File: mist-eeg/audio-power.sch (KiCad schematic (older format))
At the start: 18 parts, among them U2 LT3042xMSE, U3 LT3042xMSE

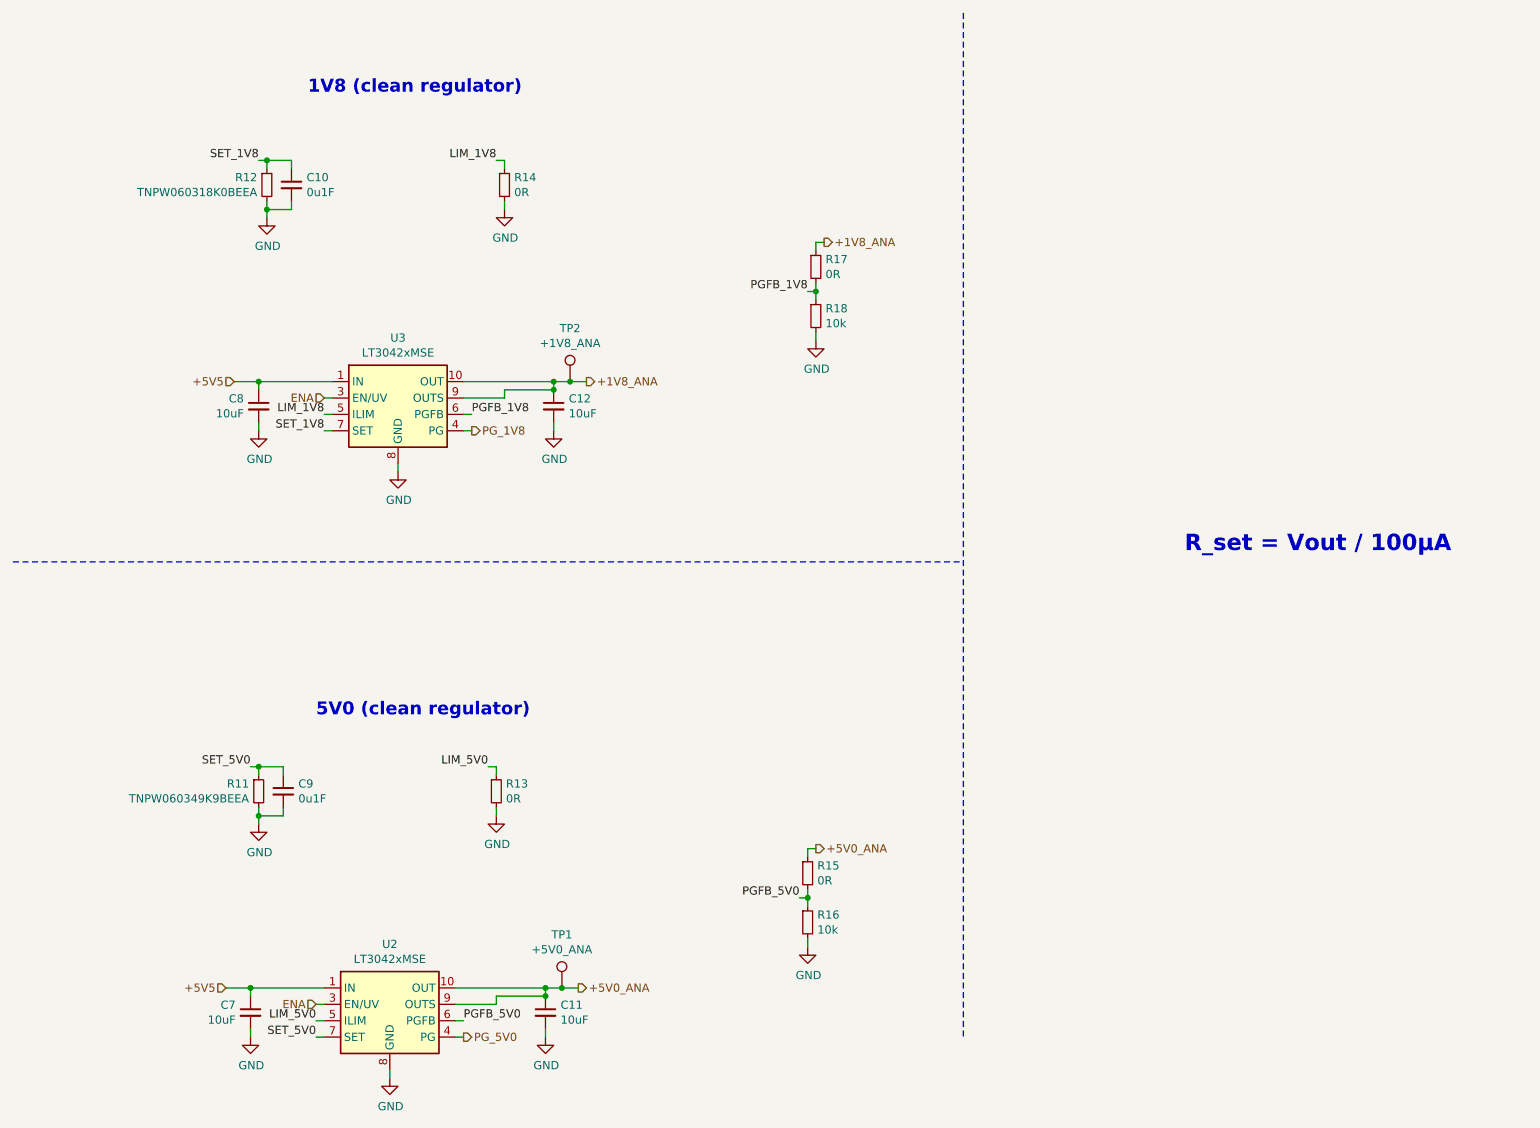
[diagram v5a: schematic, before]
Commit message: Switch to POL switching regulator to accelerate production of the board
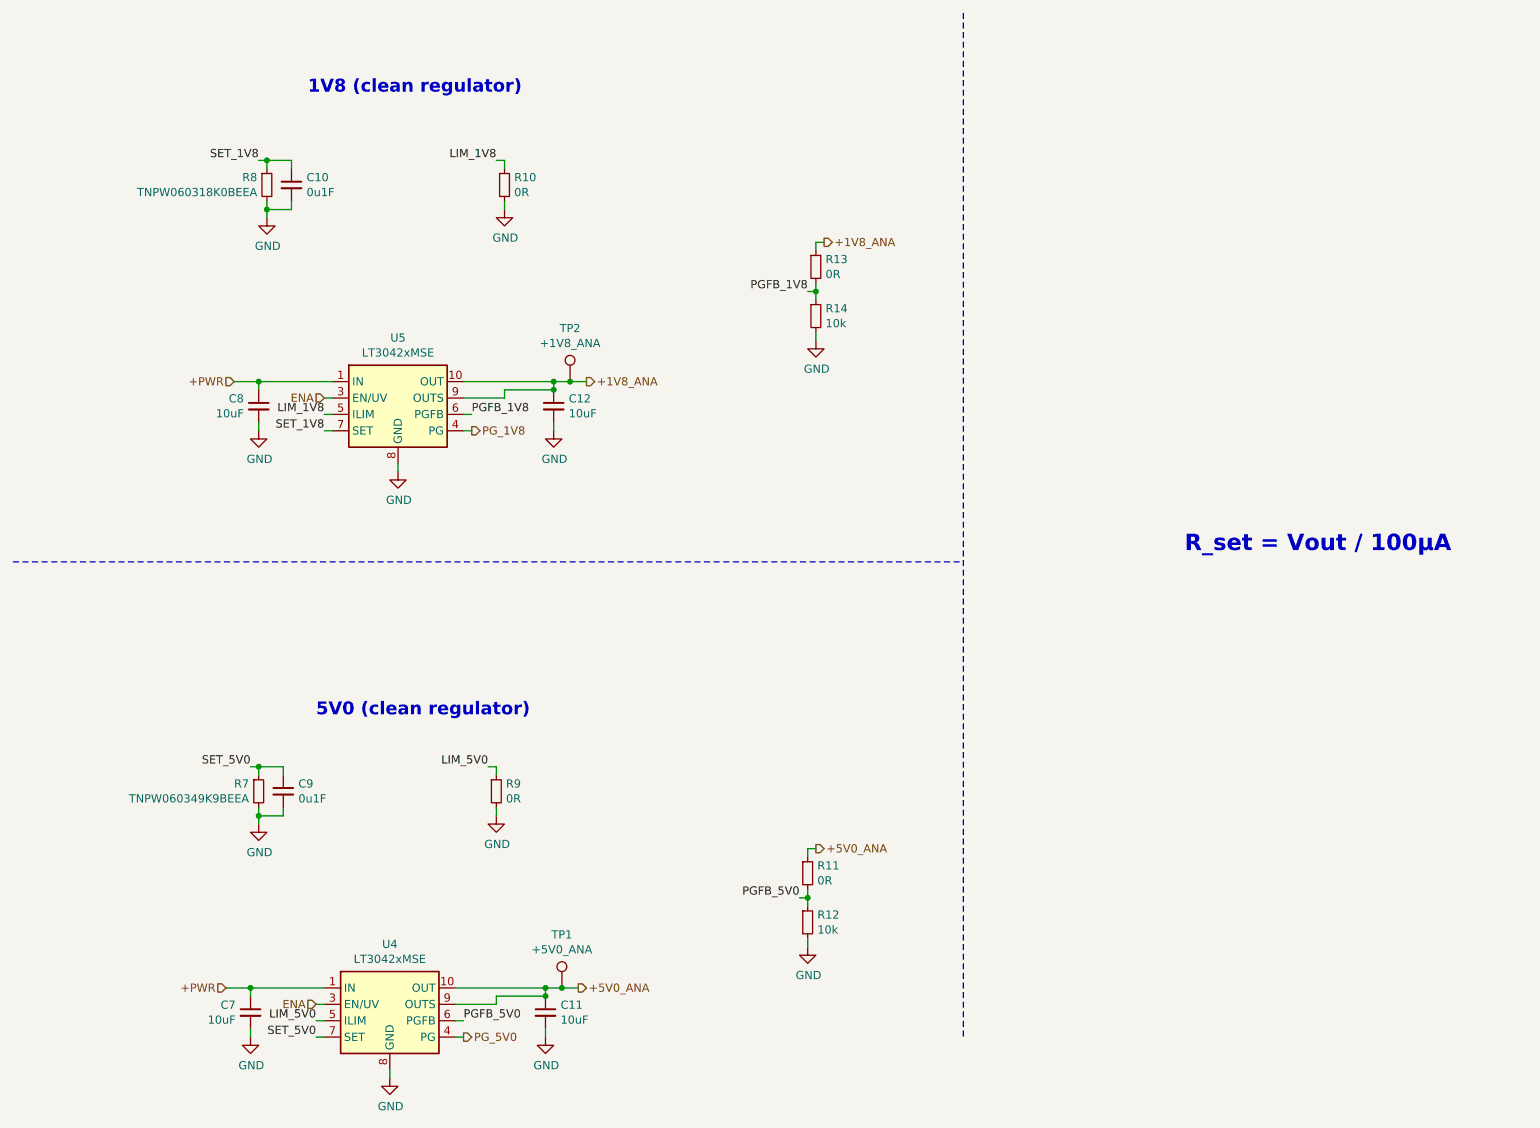
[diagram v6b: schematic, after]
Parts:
- renumbered R14 to R10, R15 to R11, R16 to R12, R17 to R13, R18 to R14, R11 to R7, R12 to R8, R13 to R9, U2 to U4, U3 to U5
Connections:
- net +5V5 renamed +PWR
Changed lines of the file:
@@
 $Descr USLetter 11000 8500
 encoding utf-8
-Sheet 4 11
+Sheet 3 8
 Title "Portiloop"
-Date "2021-08-03"
-Rev "1D"
+Date "2021-08-05"
+Rev "1E"
 Comp "MIST Lab"
 Comment1 "Designed by Xavier L'Heureux"
@@
 $EndDescr
 $Comp
-L Regulator_Linear:LT3042xMSE U3
+L Regulator_Linear:LT3042xMSE U5
 U 1 1 60CC3292
 P 2850 2850
-F 0 "U3" H 2850 3217 50  0000 C CNN
+F 0 "U5" H 2850 3217 50  0000 C CNN
 F 1 "LT3042xMSE" H 2850 3126 50  0000 C CNN
 F 2 "Package_SO:MSOP-10-1EP_3x3mm_P0.5mm_EP1.68x1.88mm" H 2850 3175 50  0001 C CNN
@@
 $EndComp
 Text HLabel 1850 2750 0    50   Input ~ 0
-+5V5
++PWR
 Text HLabel 5450 1900 2    50   Output ~ 0
 +1V8_ANA
@@
 	2400 2950 2450 2950
 $Comp
-L Device:R_Small R14
+L Device:R_Small R10
 U 1 1 60CFCD89
 P 3500 1550
-F 0 "R14" H 3559 1596 50  0000 L CNN
+F 0 "R10" H 3559 1596 50  0000 L CNN
 F 1 "0R" H 3559 1505 50  0000 L CNN
 F 2 "Resistor_SMD:R_0603_1608Metric" H 3500 1550 50  0001 C CNN
@@
 $EndComp
 $Comp
-L Device:R_Small R17
+L Device:R_Small R13
 U 1 1 60D00084
 P 5400 2050
-F 0 "R17" H 5459 2096 50  0000 L CNN
+F 0 "R13" H 5459 2096 50  0000 L CNN
 F 1 "0R" H 5459 2005 50  0000 L CNN
 F 2 "Resistor_SMD:R_0603_1608Metric" H 5400 2050 50  0001 C CNN
@@
 $EndComp
 $Comp
-L Device:R_Small R18
+L Device:R_Small R14
 U 1 1 60D0018E
 P 5400 2350
-F 0 "R18" H 5459 2396 50  0000 L CNN
+F 0 "R14" H 5459 2396 50  0000 L CNN
 F 1 "10k" H 5459 2305 50  0000 L CNN
 F 2 "Resistor_SMD:R_0603_1608Metric" H 5400 2350 50  0001 C CNN
@@
 	3500 1700 3500 1650
 $Comp
-L Device:R_Small R12
+L Device:R_Small R8
 U 1 1 60D04DA7
 P 2050 1550
-F 0 "R12" H 1991 1596 50  0000 R CNN
+F 0 "R8" H 1991 1596 50  0000 R CNN
 F 1 "TNPW060318K0BEEA" H 1991 1505 50  0000 R CNN
 F 2 "Resistor_SMD:R_0603_1608Metric" H 2050 1550 50  0001 C CNN
@@
 R_set = Vout / 100μA
 $Comp
-L Regulator_Linear:LT3042xMSE U2
+L Regulator_Linear:LT3042xMSE U4
 U 1 1 60D644F1
 P 2800 6550
-F 0 "U2" H 2800 6917 50  0000 C CNN
+F 0 "U4" H 2800 6917 50  0000 C CNN
 F 1 "LT3042xMSE" H 2800 6826 50  0000 C CNN
 F 2 "Package_SO:MSOP-10-1EP_3x3mm_P0.5mm_EP1.68x1.88mm" H 2800 6875 50  0001 C CNN
@@
 $EndComp
 Text HLabel 1800 6450 0    50   Input ~ 0
-+5V5
++PWR
 Text HLabel 5400 5600 2    50   Output ~ 0
 +5V0_ANA
@@
 	2350 6650 2400 6650
 $Comp
-L Device:R_Small R13
+L Device:R_Small R9
 U 1 1 60D64530
 P 3450 5250
-F 0 "R13" H 3509 5296 50  0000 L CNN
+F 0 "R9" H 3509 5296 50  0000 L CNN
 F 1 "0R" H 3509 5205 50  0000 L CNN
 F 2 "Resistor_SMD:R_0603_1608Metric" H 3450 5250 50  0001 C CNN
@@
 $EndComp
 $Comp
-L Device:R_Small R15
+L Device:R_Small R11
 U 1 1 60D64536
 P 5350 5750
-F 0 "R15" H 5409 5796 50  0000 L CNN
+F 0 "R11" H 5409 5796 50  0000 L CNN
 F 1 "0R" H 5409 5705 50  0000 L CNN
 F 2 "Resistor_SMD:R_0603_1608Metric" H 5350 5750 50  0001 C CNN
@@
 $EndComp
 $Comp
-L Device:R_Small R16
+L Device:R_Small R12
 U 1 1 60D6453C
 P 5350 6050
-F 0 "R16" H 5409 6096 50  0000 L CNN
+F 0 "R12" H 5409 6096 50  0000 L CNN
 F 1 "10k" H 5409 6005 50  0000 L CNN
 F 2 "Resistor_SMD:R_0603_1608Metric" H 5350 6050 50  0001 C CNN
@@
 	3450 5400 3450 5350
 $Comp
-L Device:R_Small R11
+L Device:R_Small R7
 U 1 1 60D6454C
 P 2000 5250
-F 0 "R11" H 1941 5296 50  0000 R CNN
+F 0 "R7" H 1941 5296 50  0000 R CNN
 F 1 "TNPW060349K9BEEA" H 1941 5205 50  0000 R CNN
 F 2 "Resistor_SMD:R_0603_1608Metric" H 2000 5250 50  0001 C CNN
@@
 ENA
 $Comp
-L power:GND #PWR023
+L power:GND #PWR024
 U 1 1 610B067C
 P 3800 3050
-F 0 "#PWR023" H 3800 2800 50  0001 C CNN
+F 0 "#PWR024" H 3800 2800 50  0001 C CNN
 F 1 "GND" H 3805 2877 50  0000 C CNN
 F 2 "" H 3800 3050 50  0001 C CNN
@@
 $EndComp
 $Comp
-L power:GND #PWR019
+L power:GND #PWR020
 U 1 1 610B0AB0
 P 2850 3300
-F 0 "#PWR019" H 2850 3050 50  0001 C CNN
+F 0 "#PWR020" H 2850 3050 50  0001 C CNN
 F 1 "GND" H 2855 3127 50  0000 C CNN
 F 2 "" H 2850 3300 50  0001 C CNN
@@
 $EndComp
 $Comp
-L power:GND #PWR015
+L power:GND #PWR016
 U 1 1 610B0EE6
 P 2000 3050
-F 0 "#PWR015" H 2000 2800 50  0001 C CNN
+F 0 "#PWR016" H 2000 2800 50  0001 C CNN
 F 1 "GND" H 2005 2877 50  0000 C CNN
 F 2 "" H 2000 3050 50  0001 C CNN
@@
 $EndComp
 $Comp
-L power:GND #PWR025
+L power:GND #PWR026
 U 1 1 610B1308
 P 5400 2500
-F 0 "#PWR025" H 5400 2250 50  0001 C CNN
+F 0 "#PWR026" H 5400 2250 50  0001 C CNN
 F 1 "GND" H 5405 2327 50  0000 C CNN
 F 2 "" H 5400 2500 50  0001 C CNN
@@
 $EndComp
 $Comp
-L power:GND #PWR021
+L power:GND #PWR022
 U 1 1 610B1758
 P 3500 1700
-F 0 "#PWR021" H 3500 1450 50  0001 C CNN
+F 0 "#PWR022" H 3500 1450 50  0001 C CNN
 F 1 "GND" H 3505 1527 50  0000 C CNN
 F 2 "" H 3500 1700 50  0001 C CNN
@@
 $EndComp
 $Comp
-L power:GND #PWR017
+L power:GND #PWR018
 U 1 1 610B1BAA
 P 2050 1750
-F 0 "#PWR017" H 2050 1500 50  0001 C CNN
+F 0 "#PWR018" H 2050 1500 50  0001 C CNN
 F 1 "GND" H 2055 1577 50  0000 C CNN
 F 2 "" H 2050 1750 50  0001 C CNN
@@
 $EndComp
 $Comp
-L power:GND #PWR016
+L power:GND #PWR017
 U 1 1 610B1FD2
 P 2000 5450
-F 0 "#PWR016" H 2000 5200 50  0001 C CNN
+F 0 "#PWR017" H 2000 5200 50  0001 C CNN
 F 1 "GND" H 2005 5277 50  0000 C CNN
 F 2 "" H 2000 5450 50  0001 C CNN
@@
 $EndComp
 $Comp
-L power:GND #PWR020
+L power:GND #PWR021
 U 1 1 610B2412
 P 3450 5400
-F 0 "#PWR020" H 3450 5150 50  0001 C CNN
+F 0 "#PWR021" H 3450 5150 50  0001 C CNN
 F 1 "GND" H 3455 5227 50  0000 C CNN
 F 2 "" H 3450 5400 50  0001 C CNN
@@
 $EndComp
 $Comp
-L power:GND #PWR024
+L power:GND #PWR025
 U 1 1 610B2854
 P 5350 6200
-F 0 "#PWR024" H 5350 5950 50  0001 C CNN
+F 0 "#PWR025" H 5350 5950 50  0001 C CNN
 F 1 "GND" H 5355 6027 50  0000 C CNN
 F 2 "" H 5350 6200 50  0001 C CNN
@@
 $EndComp
 $Comp
-L power:GND #PWR022
+L power:GND #PWR023
 U 1 1 610B2C71
 P 3750 6750
-F 0 "#PWR022" H 3750 6500 50  0001 C CNN
+F 0 "#PWR023" H 3750 6500 50  0001 C CNN
 F 1 "GND" H 3755 6577 50  0000 C CNN
 F 2 "" H 3750 6750 50  0001 C CNN
@@
 $EndComp
 $Comp
-L power:GND #PWR018
+L power:GND #PWR019
 U 1 1 610B30B7
 P 2800 7000
-F 0 "#PWR018" H 2800 6750 50  0001 C CNN
+F 0 "#PWR019" H 2800 6750 50  0001 C CNN
 F 1 "GND" H 2805 6827 50  0000 C CNN
 F 2 "" H 2800 7000 50  0001 C CNN
@@
 $EndComp
 $Comp
-L power:GND #PWR014
+L power:GND #PWR015
 U 1 1 610B34FF
 P 1950 6750
-F 0 "#PWR014" H 1950 6500 50  0001 C CNN
+F 0 "#PWR015" H 1950 6500 50  0001 C CNN
 F 1 "GND" H 1955 6577 50  0000 C CNN
 F 2 "" H 1950 6750 50  0001 C CNN
